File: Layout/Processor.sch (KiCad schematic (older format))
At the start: 7 parts, among them SW1 SW_Push, U1 DSPIC33FJ128GP802-I_SO

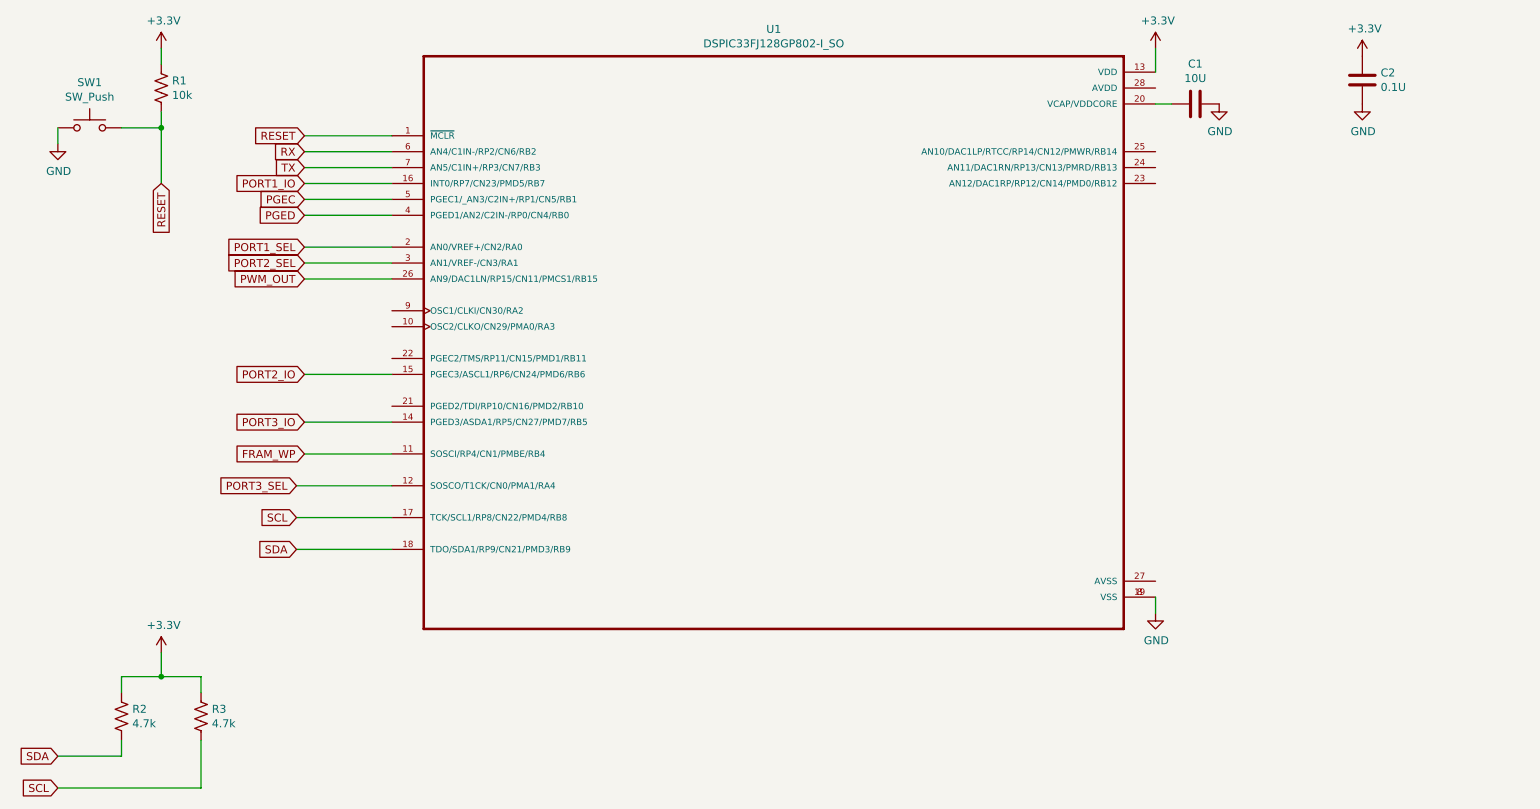
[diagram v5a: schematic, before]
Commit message: Change processor to something with a different package
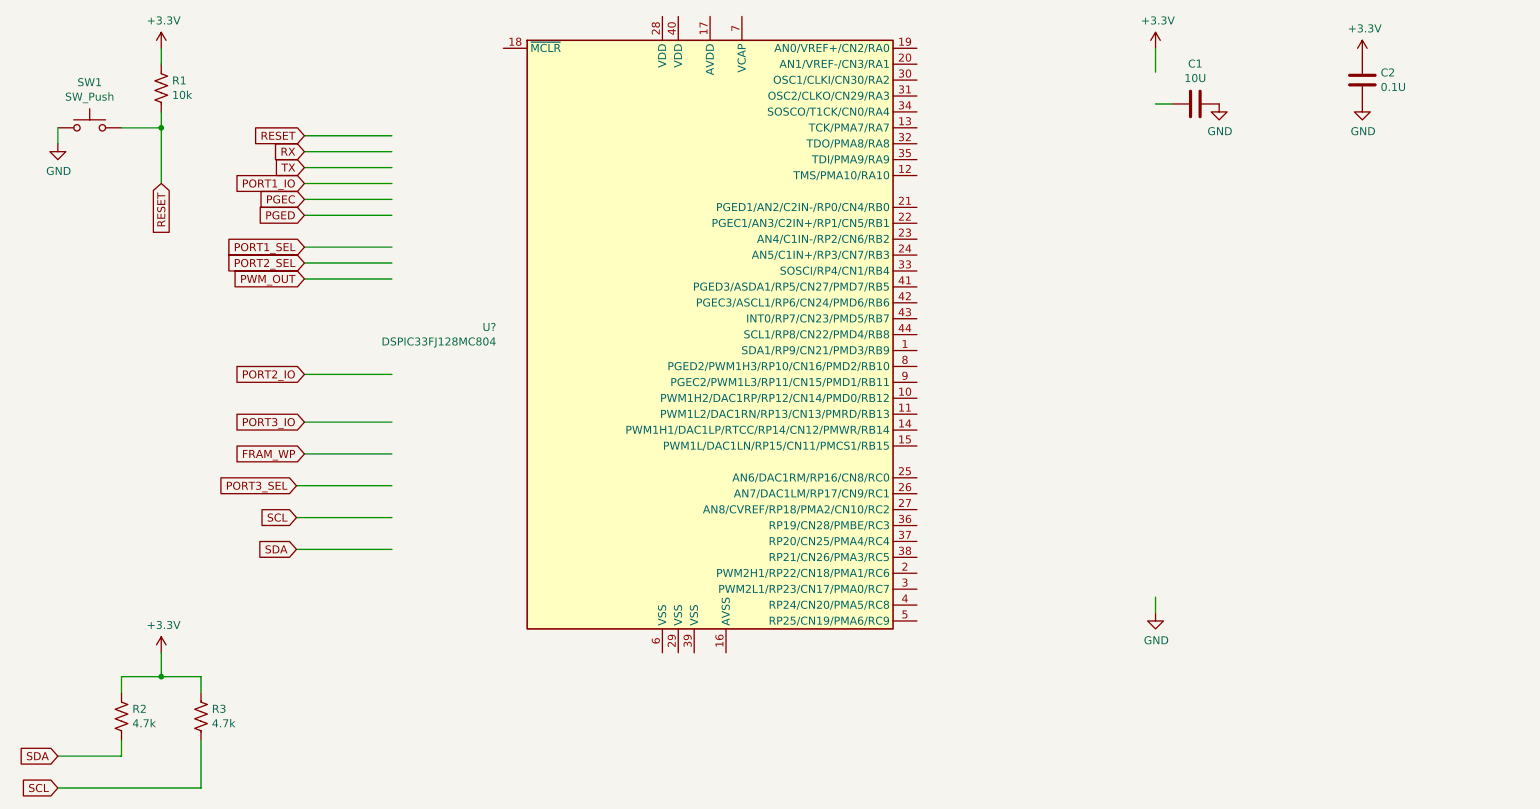
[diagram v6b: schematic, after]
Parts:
- removed U1: DSPIC33FJ128GP802-I_SO, SOIC127P1030X265-28N, symbol DSPIC33FJ128GP802-I_SO:DSPIC33FJ128GP802-I_SO
- added U?: DSPIC33FJ128MC804, symbol DSP_Microchip_DSPIC33:DSPIC33FJ128MC804
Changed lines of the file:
@@
 Text GLabel 1950 2000 3    50   Input ~ 0
 RESET
-$Comp
-L DSPIC33FJ128GP802-I_SO:DSPIC33FJ128GP802-I_SO U1
-U 1 1 5F360275
-P 5800 3000
-F 0 "U1" H 5800 4970 50  0000 C CNN
-F 1 "DSPIC33FJ128GP802-I_SO" H 5800 4879 50  0000 C CNN
-F 2 "SOIC127P1030X265-28N" H 5800 3000 50  0001 L BNN
-F 3 "" H 5800 3000 50  0001 C CNN
-	1    5800 3000
-	1    0    0    -1
-$EndComp
 Wire Wire Line
 	3400 1700 2850 1700
@@
 Wire Wire Line
 	2850 3700 3400 3700
+$Comp
+L DSP_Microchip_DSPIC33:DSPIC33FJ128MC804 U?
+U 1 1 5F5844E5
+P 5400 2950
+F 0 "U?" H 4056 2996 50  0000 R CNN
+F 1 "DSPIC33FJ128MC804" H 4056 2905 50  0000 R CNN
+F 2 "" H 5400 2950 50  0001 C CNN
+F 3 "http://ww1.microchip.com/downloads/en/DeviceDoc/70291G.pdf" H 5400 2950 50  0001 C CNN
+	1    5400 2950
+	1    0    0    -1
+$EndComp
 $EndSCHEMATC

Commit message: Remap IO
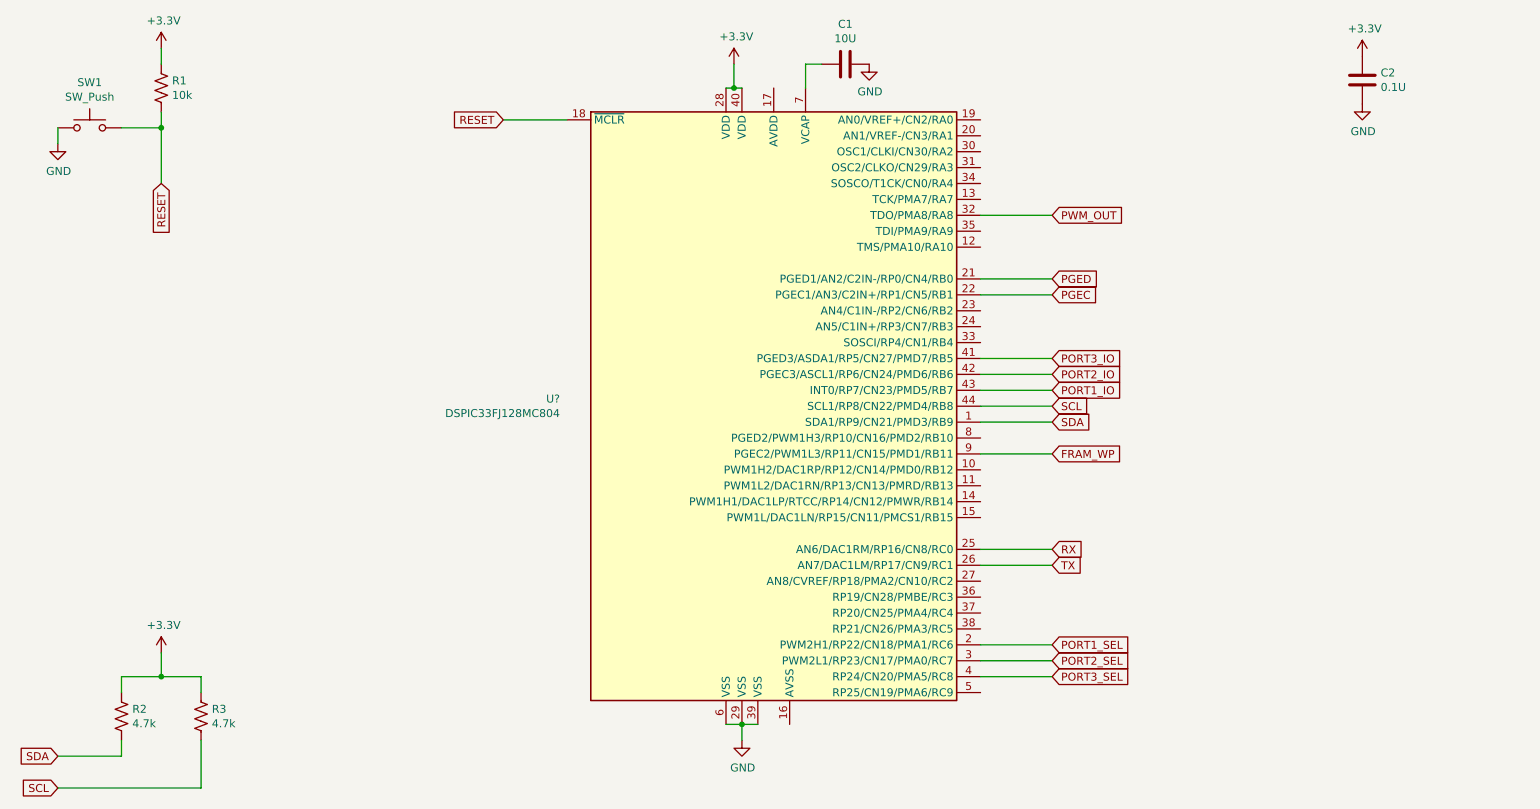
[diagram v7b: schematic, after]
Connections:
- wire segments 32 -> 37
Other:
- moved on the sheet: C1, U?
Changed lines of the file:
@@
 Text GLabel 1950 2000 3    50   Input ~ 0
 RESET
-Wire Wire Line
-	3400 1700 2850 1700
-Text GLabel 2850 1700 0    50   Input ~ 0
+Text GLabel 4100 1600 0    50   Input ~ 0
 RESET
 $Comp
 L Device:C C1
 U 1 1 5F36AEA4
-P 8450 1500
-F 0 "C1" V 8198 1500 50  0000 C CNN
-F 1 "10U" V 8289 1500 50  0000 C CNN
-F 2 "Capacitor_SMD:C_0603_1608Metric_Pad1.05x0.95mm_HandSolder" H 8488 1350 50  0001 C CNN
-F 3 "~" H 8450 1500 50  0001 C CNN
-	1    8450 1500
+P 6250 1250
+F 0 "C1" V 5998 1250 50  0000 C CNN
+F 1 "10U" V 6089 1250 50  0000 C CNN
+F 2 "Capacitor_SMD:C_0603_1608Metric_Pad1.05x0.95mm_HandSolder" H 6288 1100 50  0001 C CNN
+F 3 "~" H 6250 1250 50  0001 C CNN
+	1    6250 1250
 	0    1    1    0
 $EndComp
 Wire Wire Line
-	8200 1500 8300 1500
+	6000 1250 6100 1250
 $Comp
 L power:+3.3V #PWR0103
 U 1 1 5F36B77A
-P 8200 1150
-F 0 "#PWR0103" H 8200 1000 50  0001 C CNN
-F 1 "+3.3V" H 8215 1323 50  0000 C CNN
-F 2 "" H 8200 1150 50  0001 C CNN
-F 3 "" H 8200 1150 50  0001 C CNN
-	1    8200 1150
-	1    0    0    -1
-$EndComp
-Wire Wire Line
-	8200 1150 8200 1300
+P 5550 1250
+F 0 "#PWR0103" H 5550 1100 50  0001 C CNN
+F 1 "+3.3V" H 5565 1423 50  0000 C CNN
+F 2 "" H 5550 1250 50  0001 C CNN
+F 3 "" H 5550 1250 50  0001 C CNN
+	1    5550 1250
+	1    0    0    -1
+$EndComp
 $Comp
 L power:GND #PWR0104
 U 1 1 5F36C154
-P 8600 1500
-F 0 "#PWR0104" H 8600 1250 50  0001 C CNN
-F 1 "GND" H 8605 1327 50  0000 C CNN
-F 2 "" H 8600 1500 50  0001 C CNN
-F 3 "" H 8600 1500 50  0001 C CNN
-	1    8600 1500
+P 6400 1250
+F 0 "#PWR0104" H 6400 1000 50  0001 C CNN
+F 1 "GND" H 6405 1077 50  0000 C CNN
+F 2 "" H 6400 1250 50  0001 C CNN
+F 3 "" H 6400 1250 50  0001 C CNN
+	1    6400 1250
 	1    0    0    -1
 $EndComp
@@
 L power:GND #PWR0105
 U 1 1 5F36C44E
-P 8200 4700
-F 0 "#PWR0105" H 8200 4450 50  0001 C CNN
-F 1 "GND" H 8205 4527 50  0000 C CNN
-F 2 "" H 8200 4700 50  0001 C CNN
-F 3 "" H 8200 4700 50  0001 C CNN
-	1    8200 4700
-	1    0    0    -1
-$EndComp
-Wire Wire Line
-	8200 4700 8200 4600
-Wire Wire Line
-	3400 4100 2800 4100
-Wire Wire Line
-	3400 4300 2800 4300
-Text GLabel 2800 4100 0    50   Input ~ 0
+P 5600 5500
+F 0 "#PWR0105" H 5600 5250 50  0001 C CNN
+F 1 "GND" H 5605 5327 50  0000 C CNN
+F 2 "" H 5600 5500 50  0001 C CNN
+F 3 "" H 5600 5500 50  0001 C CNN
+	1    5600 5500
+	1    0    0    -1
+$EndComp
+Text GLabel 7550 3400 2    50   Input ~ 0
 SCL
-Text GLabel 2800 4300 0    50   Input ~ 0
+Text GLabel 7550 3500 2    50   Input ~ 0
 SDA
-Wire Wire Line
-	3400 2000 2850 2000
-Wire Wire Line
-	3400 2100 2850 2100
-Wire Wire Line
-	3400 2200 2850 2200
-Text GLabel 2850 2100 0    50   Input ~ 0
+Text GLabel 7550 2700 2    50   Input ~ 0
 PGEC
-Text GLabel 2850 2200 0    50   Input ~ 0
+Text GLabel 7550 2600 2    50   Input ~ 0
 PGED
-Text GLabel 2850 2000 0    50   Input ~ 0
+Text GLabel 7550 3300 2    50   Input ~ 0
 PORT1_IO
-Wire Wire Line
-	3400 3200 2850 3200
-Wire Wire Line
-	3400 3500 2850 3500
-Text GLabel 2850 3200 0    50   Input ~ 0
+Text GLabel 7550 3200 2    50   Input ~ 0
 PORT2_IO
-Text GLabel 2850 3500 0    50   Input ~ 0
+Text GLabel 7550 3100 2    50   Input ~ 0
 PORT3_IO
-Wire Wire Line
-	3400 1900 2850 1900
-Wire Wire Line
-	3400 1800 2850 1800
-Text GLabel 2850 1800 0    50   Input ~ 0
+Text GLabel 7550 4300 2    50   Input ~ 0
 RX
-Text GLabel 2850 1900 0    50   Input ~ 0
+Text GLabel 7550 4400 2    50   Input ~ 0
 TX
-Wire Wire Line
-	3400 2600 2850 2600
-Text GLabel 2850 2600 0    50   Input ~ 0
+Text GLabel 7550 2200 2    50   Input ~ 0
 PWM_OUT
-Wire Wire Line
-	3400 2400 2850 2400
-Wire Wire Line
-	3400 2500 2850 2500
-Text GLabel 2850 2400 0    50   Input ~ 0
+Text GLabel 7550 4900 2    50   Input ~ 0
 PORT1_SEL
-Text GLabel 2850 2500 0    50   Input ~ 0
+Text GLabel 7550 5000 2    50   Input ~ 0
 PORT2_SEL
-Wire Wire Line
-	3400 3900 2800 3900
-Text GLabel 2800 3900 0    50   Input ~ 0
+Text GLabel 7550 5100 2    50   Input ~ 0
 PORT3_SEL
 $Comp
@@
 Wire Wire Line
 	1950 5100 2200 5100
-Text GLabel 2850 3700 0    50   Input ~ 0
+Text GLabel 7550 3700 2    50   Input ~ 0
 FRAM_WP
-Wire Wire Line
-	2850 3700 3400 3700
 $Comp
 L DSP_Microchip_DSPIC33:DSPIC33FJ128MC804 U?
 U 1 1 5F5844E5
-P 5400 2950
-F 0 "U?" H 4056 2996 50  0000 R CNN
-F 1 "DSPIC33FJ128MC804" H 4056 2905 50  0000 R CNN
-F 2 "" H 5400 2950 50  0001 C CNN
-F 3 "http://ww1.microchip.com/downloads/en/DeviceDoc/70291G.pdf" H 5400 2950 50  0001 C CNN
-	1    5400 2950
-	1    0    0    -1
-$EndComp
+P 5800 3400
+F 0 "U?" H 4456 3446 50  0000 R CNN
+F 1 "DSPIC33FJ128MC804" H 4456 3355 50  0000 R CNN
+F 2 "" H 5800 3400 50  0001 C CNN
+F 3 "http://ww1.microchip.com/downloads/en/DeviceDoc/70291G.pdf" H 5800 3400 50  0001 C CNN
+	1    5800 3400
+	1    0    0    -1
+$EndComp
+Wire Wire Line
+	5500 5400 5600 5400
+Wire Wire Line
+	5600 5400 5700 5400
+Connection ~ 5600 5400
+Wire Wire Line
+	5500 1400 5550 1400
+Wire Wire Line
+	7100 3300 7550 3300
+Wire Wire Line
+	7100 3400 7550 3400
+Wire Wire Line
+	7100 3500 7550 3500
+Wire Wire Line
+	7100 3200 7550 3200
+Wire Wire Line
+	7100 3100 7550 3100
+Wire Wire Line
+	4100 1600 4500 1600
+Wire Wire Line
+	7100 2600 7550 2600
+Wire Wire Line
+	7100 2700 7550 2700
+Wire Wire Line
+	7100 4300 7550 4300
+Wire Wire Line
+	7100 4400 7550 4400
+Wire Wire Line
+	7100 4900 7550 4900
+Wire Wire Line
+	7100 5000 7550 5000
+Wire Wire Line
+	7100 5100 7550 5100
+Wire Wire Line
+	7550 3700 7100 3700
+Wire Wire Line
+	7550 2200 7100 2200
+Wire Wire Line
+	5550 1250 5550 1400
+Connection ~ 5550 1400
+Wire Wire Line
+	5550 1400 5600 1400
+Wire Wire Line
+	6000 1250 6000 1400
+Wire Wire Line
+	5600 5500 5600 5400
 $EndSCHEMATC

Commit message: Priliminary PCB layout
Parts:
- added J5, J6: Conn_01x02_Female, Connector_PinSocket_2.54mm:PinSocket_1x02_P2.54mm_Vertical, symbol Connector:Conn_01x02_Female
- U1: renamed from U?; footprint (none) -> Package_QFP:TQFP-44_10x10mm_P0.8mm
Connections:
- net RX: now also J5.1 (Pin_1)
- net SCL: now also J6.1 (Pin_1)
- net SDA: now also J6.2 (Pin_2)
- net TX: now also J5.2 (Pin_2)
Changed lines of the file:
@@
 FRAM_WP
 $Comp
-L DSP_Microchip_DSPIC33:DSPIC33FJ128MC804 U?
+L DSP_Microchip_DSPIC33:DSPIC33FJ128MC804 U1
 U 1 1 5F5844E5
 P 5800 3400
-F 0 "U?" H 4456 3446 50  0000 R CNN
+F 0 "U1" H 4456 3446 50  0000 R CNN
 F 1 "DSPIC33FJ128MC804" H 4456 3355 50  0000 R CNN
-F 2 "" H 5800 3400 50  0001 C CNN
+F 2 "Package_QFP:TQFP-44_10x10mm_P0.8mm" H 5800 3400 50  0001 C CNN
 F 3 "http://ww1.microchip.com/downloads/en/DeviceDoc/70291G.pdf" H 5800 3400 50  0001 C CNN
 	1    5800 3400
@@
 Wire Wire Line
 	5600 5500 5600 5400
+$Comp
+L Connector:Conn_01x02_Female J5
+U 1 1 5F5B5019
+P 9650 2750
+F 0 "J5" H 9678 2726 50  0000 L CNN
+F 1 "Conn_01x02_Female" H 9678 2635 50  0000 L CNN
+F 2 "Connector_PinSocket_2.54mm:PinSocket_1x02_P2.54mm_Vertical" H 9650 2750 50  0001 C CNN
+F 3 "~" H 9650 2750 50  0001 C CNN
+	1    9650 2750
+	1    0    0    -1
+$EndComp
+$Comp
+L Connector:Conn_01x02_Female J6
+U 1 1 5F5B5A51
+P 9650 3200
+F 0 "J6" H 9678 3176 50  0000 L CNN
+F 1 "Conn_01x02_Female" H 9678 3085 50  0000 L CNN
+F 2 "Connector_PinSocket_2.54mm:PinSocket_1x02_P2.54mm_Vertical" H 9650 3200 50  0001 C CNN
+F 3 "~" H 9650 3200 50  0001 C CNN
+	1    9650 3200
+	1    0    0    -1
+$EndComp
+Wire Wire Line
+	9450 2750 9150 2750
+Wire Wire Line
+	9450 2850 9150 2850
+Wire Wire Line
+	9450 3200 9150 3200
+Wire Wire Line
+	9450 3300 9150 3300
+Text GLabel 9150 2750 0    50   Input ~ 0
+RX
+Text GLabel 9150 2850 0    50   Input ~ 0
+TX
+Text GLabel 9150 3200 0    50   Input ~ 0
+SCL
+Text GLabel 9150 3300 0    50   Input ~ 0
+SDA
 $EndSCHEMATC
